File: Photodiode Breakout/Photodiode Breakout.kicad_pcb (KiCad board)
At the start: 2 copper layers, 2 parts, among them U1 OPT101, U2 Molex_SL-3

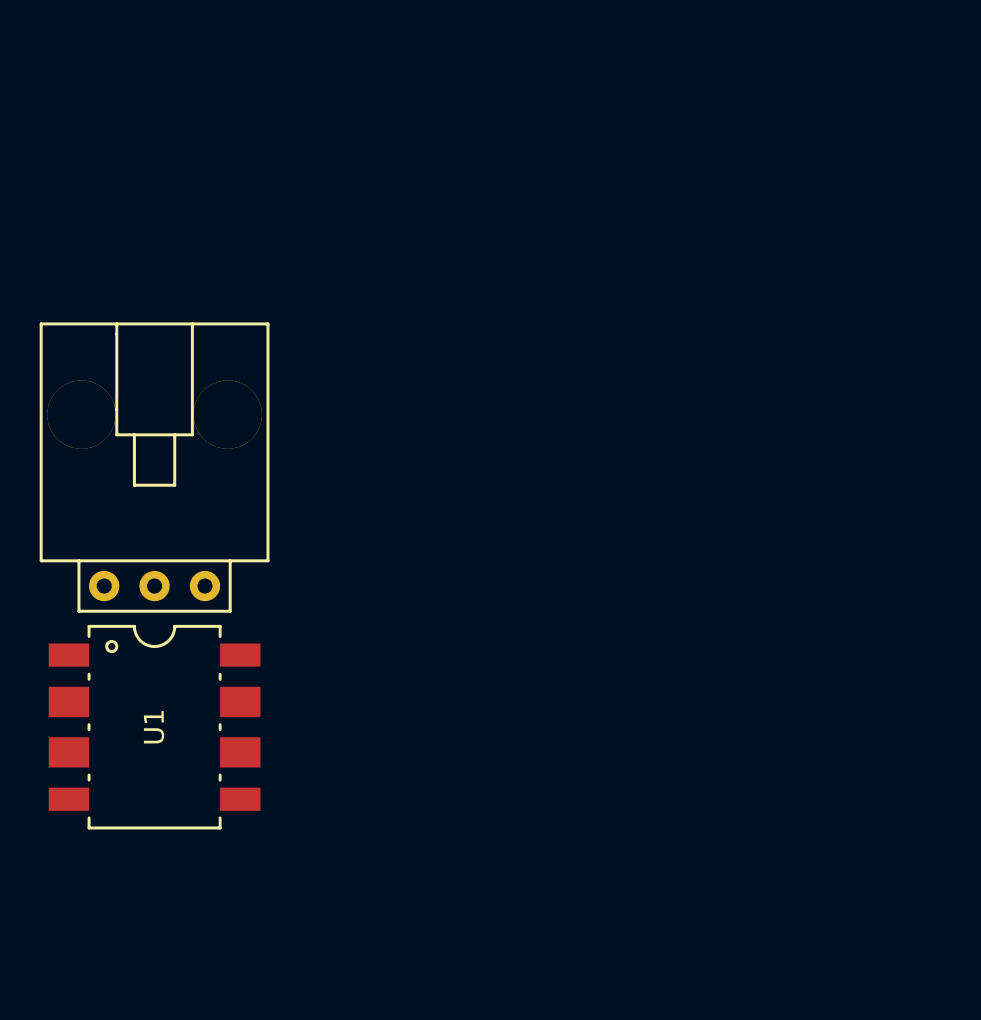
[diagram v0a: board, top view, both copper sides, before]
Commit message: Created Photodiode board
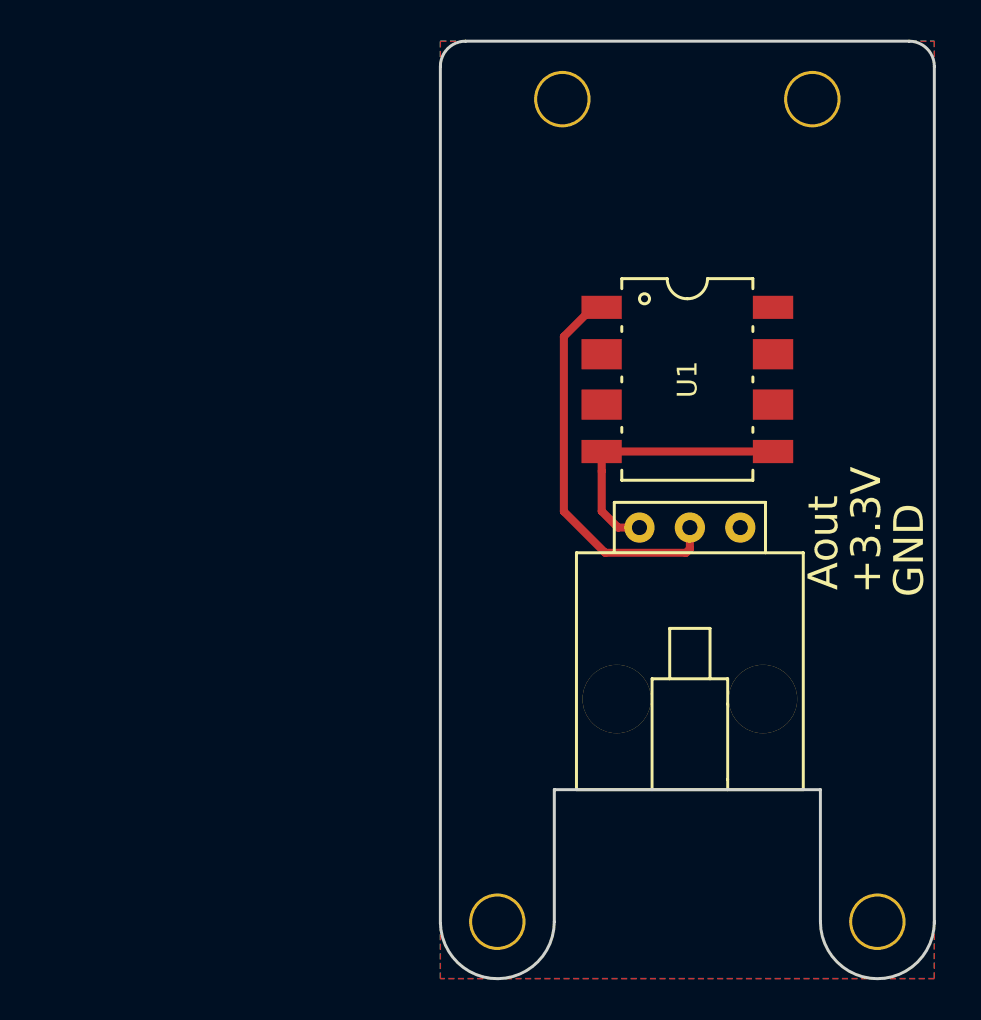
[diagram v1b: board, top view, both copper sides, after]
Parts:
- added G***: LOGO, MRDT_Silkscreens:MRDT_Logo_10mm, B.Cu at (135.5, 32.8)
- added REF**: Via_P1.27mm_5x5, MRDT_Drill_Holes:Via_.6mm, F.Cu at (146.7, 42.3)
- added REF**: Via_P1.27mm_5x5, MRDT_Drill_Holes:Via_.6mm, F.Cu at (142.9, 43.9)
- added REF**: Via_P1.27mm_5x5, MRDT_Drill_Holes:Via_.6mm, F.Cu at (146.4, 49.4)
- added REF**: Via_P1.27mm_5x5, MRDT_Drill_Holes:Via_.6mm, F.Cu at (126.0, 48.5)
- moved U1 32.1 mm to (130.2, 39.5)
- moved U2 27.1 mm to (130.3, 47.0), turned to 180 degrees
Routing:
- net /+3V3: track 0.00 -> 19.7 mm
- net /SIG: track 0.00 -> 13.9 mm
- added copper zone on B.Cu, net /GND
- added copper zone on F.Cu, net /GND
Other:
- board outline added: 24.9 x 47.2 mm
- board text added: "+3.3V"
- board text added: "Aout"
- board text added: "GND"
- board text added: "Photodiode Breakout, Rev 1 Mars Rover, 2018 Missouri S&T Andrew Van Horn"
